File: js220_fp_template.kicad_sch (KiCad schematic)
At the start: 5 parts, among them J1 JS220

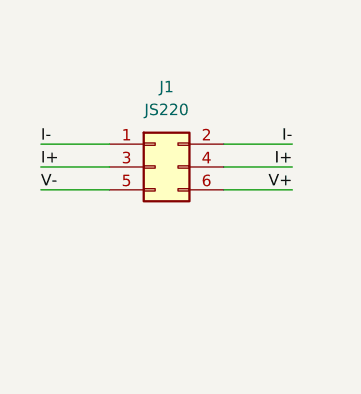
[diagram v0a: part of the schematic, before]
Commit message: Update to use JS220 symbol and locked PCB items
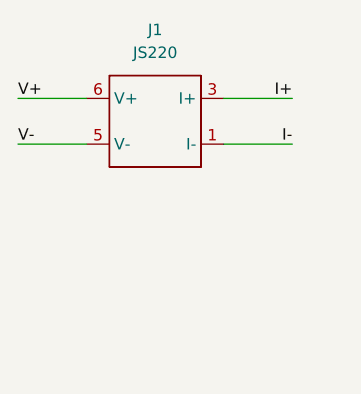
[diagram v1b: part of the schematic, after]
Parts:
- removed J1: JS220, Joulescope:SAMTEC_TSM-103-01-S-DV-A, symbol Connector_Generic:Conn_02x03_Odd_Even
- added J1: JS220, Joulescope:SAMTEC_TSM-103-01-S-DV-A, symbol Joulescope:JS220
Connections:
- net I+: now also J1.3 (I+), J1.4 (I+)
- net I-: now also J1.1 (I-), J1.2 (I-)
- net V+: now also J1.6 (V+)
- net V-: now also J1.5 (V-)
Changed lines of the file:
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@@
     (title "Joulescope JS220 Front Panel Template")
     (date "2022-10-23")
-    (rev "1.0")
+    (rev "1.1")
     (company "Alvaro Prieto")
   )
-  (wire (pts (xy 142.24 93.98) (xy 149.86 93.98))
+  (wire (pts (xy 162.56 88.9) (xy 170.18 88.9))
     (stroke (width 0) (type default) (color 0 0 0 0))
   )
-  (wire (pts (xy 142.24 96.52) (xy 149.86 96.52))
+  (wire (pts (xy 162.56 93.98) (xy 170.18 93.98))
     (stroke (width 0) (type default) (color 0 0 0 0))
   )
-  (wire (pts (xy 162.56 99.06) (xy 170.18 99.06))
-    (stroke (width 0) (type default) (color 0 0 0 0))
-  )
-  (wire (pts (xy 142.24 99.06) (xy 149.86 99.06))
-    (stroke (width 0) (type default) (color 0 0 0 0))
-  )
-  (wire (pts (xy 162.56 96.52) (xy 170.18 96.52))
+  (wire (pts (xy 147.32 88.9) (xy 139.7 88.9))
     (stroke (width 0) (type default) (color 0 0 0 0))
   )
@@
     (stroke (width 0) (type default) (color 0 0 0 0))
   )
-  (wire (pts (xy 162.56 93.98) (xy 170.18 93.98))
+  (wire (pts (xy 139.7 93.98) (xy 147.32 93.98))
     (stroke (width 0) (type default) (color 0 0 0 0))
   )
-  (label "V-" (at 142.24 99.06 0)
+  (label "I-" (at 170.18 93.98 180)
+    (effects (font (size 1.27 1.27)) (justify right bottom))
+  )
+  (label "V-" (at 139.7 93.98 0)
     (effects (font (size 1.27 1.27)) (justify left bottom))
   )
-  (label "I-" (at 142.24 93.98 0)
+  (label "V+" (at 139.7 88.9 0)
     (effects (font (size 1.27 1.27)) (justify left bottom))
-  )
-  (label "I+" (at 170.18 96.52 180)
-    (effects (font (size 1.27 1.27)) (justify right bottom))
-  )
-  (label "V+" (at 170.18 99.06 180)
-    (effects (font (size 1.27 1.27)) (justify right bottom))
   )
   (label "CH_GND" (at 172.72 193.04 180)
     (effects (font (size 1.27 1.27)) (justify right bottom))
   )
-  (label "I+" (at 142.24 96.52 0)
-    (effects (font (size 1.27 1.27)) (justify left bottom))
-  )
-  (label "I-" (at 170.18 93.98 180)
+  (label "I+" (at 170.18 88.9 180)
     (effects (font (size 1.27 1.27)) (justify right bottom))
   )
@@
       (effects (font (size 1.27 1.27)) hide)
     )
-  )
-  (symbol (lib_id "Connector_Generic:Conn_02x03_Odd_Even") (at 154.94 96.52 0) (unit 1)
-    (in_bom yes) (on_board yes) (fields_autoplaced)
-    (property "Reference" "J1" (id 0) (at 156.21 87.63 0))
-    (property "Value" "JS220" (id 1) (at 156.21 90.17 0))
-    (property "Footprint" "Joulescope:SAMTEC_TSM-103-01-S-DV-A" (id 2) (at 154.94 96.52 0)
-      (effects (font (size 1.27 1.27)) hide)
-    )
-    (property "Datasheet" "~" (id 3) (at 154.94 96.52 0)
-      (effects (font (size 1.27 1.27)) hide)
-    )
-    (property "MFG" "Samtec" (id 4) (at 154.94 96.52 0)
-      (effects (font (size 1.27 1.27)) hide)
-    )
-    (property "MPN" "TSM-103-01-S-DV-A" (id 5) (at 154.94 96.52 0)
-      (effects (font (size 1.27 1.27)) hide)
-    )
-    (pin "1")
-    (pin "2")
-    (pin "3")
-    (pin "4")
-    (pin "5")
-    (pin "6")
   )
   (symbol (lib_id "Mechanical:MountingHole") (at 157.48 180.34 0) (unit 1)
@@
     )
   )
+  (symbol (lib_id "Joulescope:JS220") (at 154.94 91.44 0) (unit 1)
+    (in_bom yes) (on_board yes) (fields_autoplaced)
+    (property "Reference" "J1" (id 0) (at 154.94 81.28 0))
+    (property "Value" "JS220" (id 1) (at 154.94 83.82 0))
+    (property "Footprint" "Joulescope:SAMTEC_TSM-103-01-S-DV-A" (id 2) (at 154.94 93.98 0)
+      (effects (font (size 1.27 1.27)) hide)
+    )
+    (property "Datasheet" "" (id 3) (at 154.94 93.98 0)
+      (effects (font (size 1.27 1.27)) hide)
+    )
+    (pin "1")
+    (pin "2")
+    (pin "3")
+    (pin "4")
+    (pin "5")
+    (pin "6")
+  )
   (sheet_instances
     (path "/" (page "1"))
@@
       (reference "H3") (unit 1) (value "MountingHole") (footprint "Joulescope:MOUNTING_HOLE_3.3MM")
     )
-    (path "/5263f378-21b2-4b9b-9912-a2484ec0d7cc"
+    (path "/ff751d8a-9305-492e-b66c-b663379c0659"
       (reference "J1") (unit 1) (value "JS220") (footprint "Joulescope:SAMTEC_TSM-103-01-S-DV-A")
     )
